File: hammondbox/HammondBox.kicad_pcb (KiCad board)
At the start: 2 copper layers, 42.5 x 29 mm, 14 parts, among them P1 USB_OTG, P2 CONN_02X03, P3 CONN_01X08, U1 ESP-12E, U2 TLV70233DBV

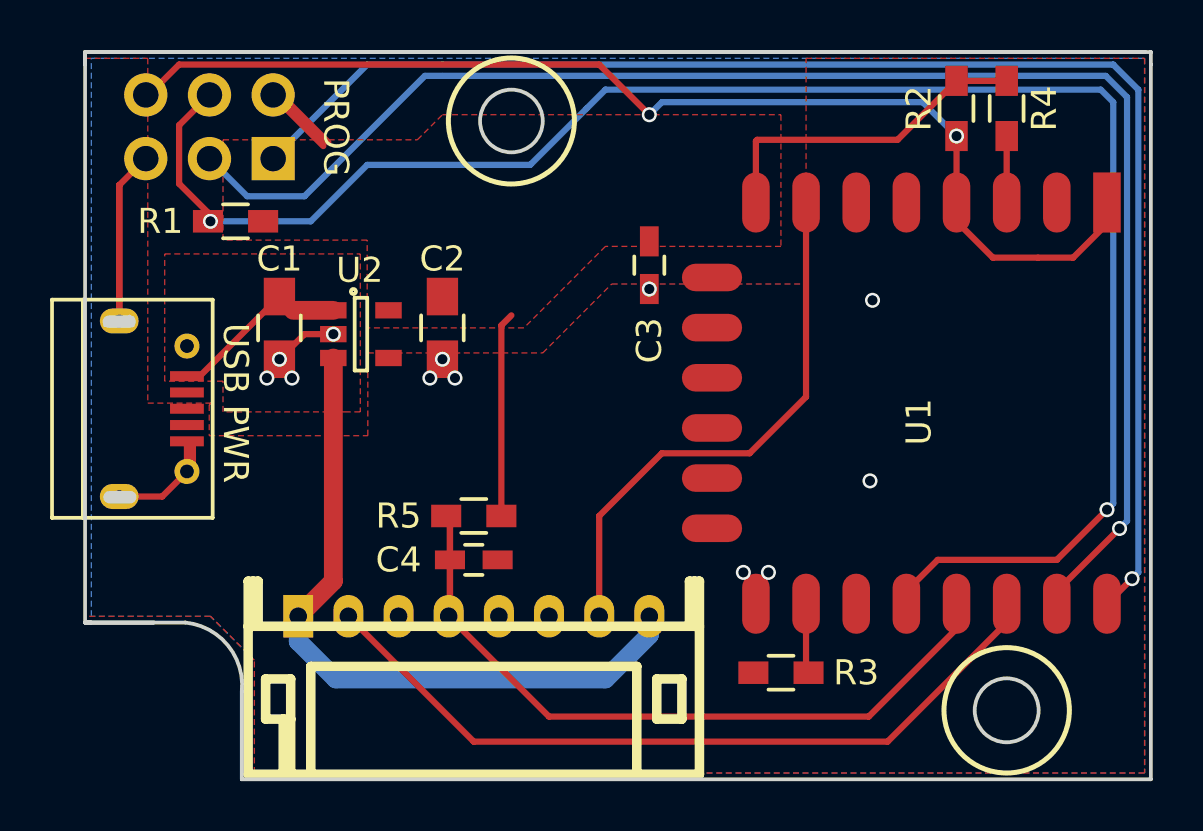
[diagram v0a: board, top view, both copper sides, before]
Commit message: Use MCP1702 for regulator, use reflow sized pads.
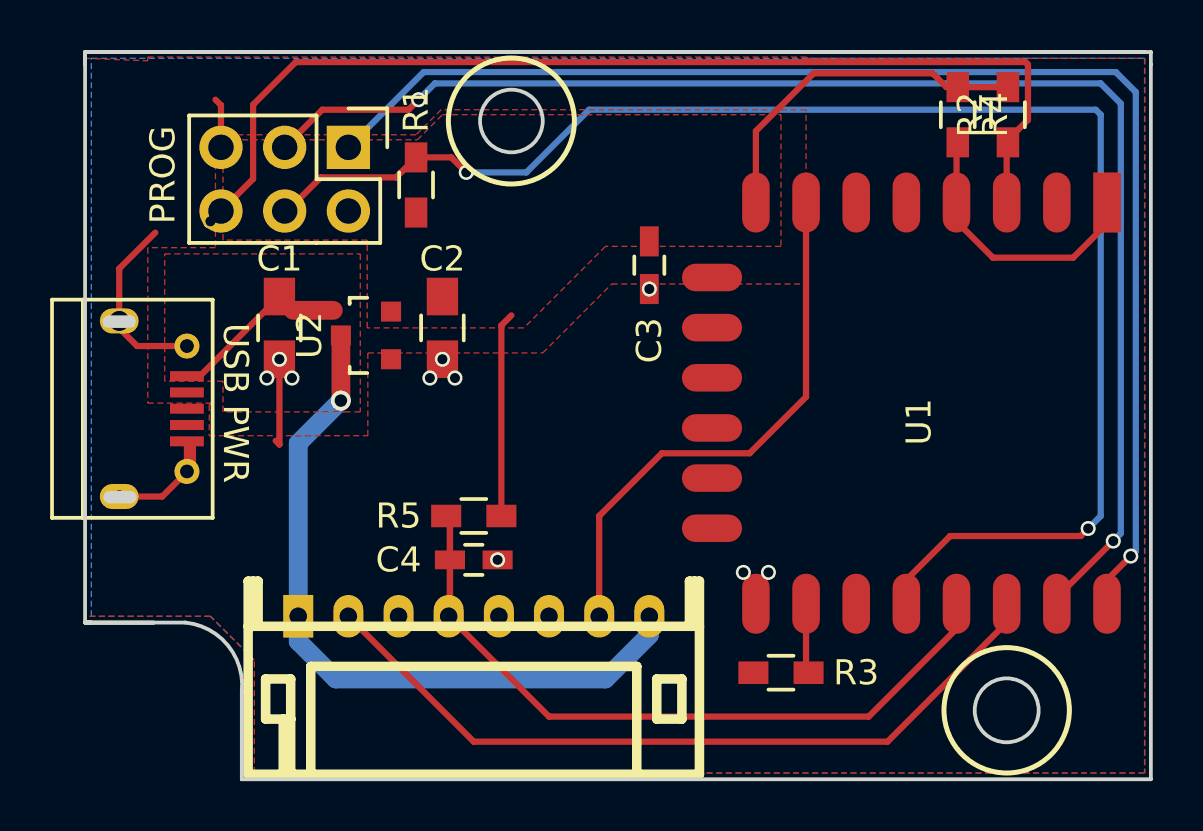
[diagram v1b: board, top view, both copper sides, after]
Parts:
- P2: moved to F.Cu
- U2: value TLV70233DBV -> AP1117D15; footprint SOT-23-5 -> TO_SOT_Packages_SMD:SOT-23
- moved R1 7.34 mm to (113.2, 55.3), turned to 90 degrees
- moved P2 3.03 mm to (110.5, 53.8), turned to 270 degrees
- moved R2 2.07 mm to (136.8, 52.5)
- moved R4 1.97 mm to (134.8, 52.5)
- moved U2 0.21 mm to (111.2, 61.3), turned to 90 degrees
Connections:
- P2 pad 6: GPIO16 -> CH_PD
- R2 pad 2: GPIO16 -> CH_PD
- R4 pad 2: Net-(R4-Pad2) -> RST
- U1 pad 1: GPIO16 -> RST
- U1 pad 3: Net-(R4-Pad2) -> CH_PD
- U1 pad 4: GPIO16 -> RST
- U2 pad 1: +5V -> GND
- U2 pad 2: GND -> +3V3
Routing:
- net GPIO16: track 45.8 -> 0.00 mm, vias 2 -> 0
- net CH_PD: track 0.00 -> 42.9 mm, vias 0 -> 1
- net RST: track 0.00 -> 11.4 mm
- net GPIO0: track 70.7 -> 61.0 mm
- net +3V3: track 27.5 -> 22.2 mm
- net RXD: track 60.9 -> 56.2 mm, vias 1 -> 2
- net TXD: track 57.5 -> 53.9 mm
- net Net-(R4-Pad2): track 2.65 -> 0.00 mm
- net GND: track 26.9 -> 25.1 mm
- net +5V: track 35.4 -> 36.4 mm, vias 0 -> 1
- net (no net): vias 2 -> 0
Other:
- board text added: "ESP HammondBox 0.4"
- board text removed: "ESP HammondBox 0.3"
